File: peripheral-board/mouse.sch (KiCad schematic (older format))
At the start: 3 parts

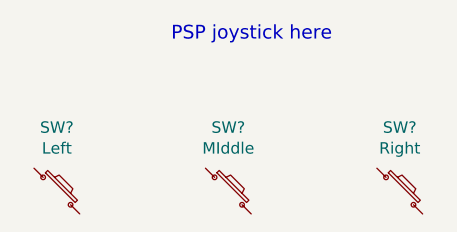
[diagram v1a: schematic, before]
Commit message: added button 3d model
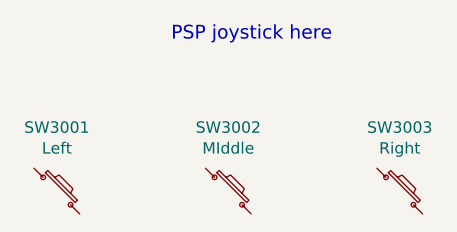
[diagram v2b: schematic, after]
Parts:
- SW3001, SW3002, SW3003: renamed from SW?; footprint (none) -> lib:SMD-TACT-5.2x5.2x2mm
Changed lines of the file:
@@
 PSP joystick here\n
 $Comp
-L SW_PUSH_Small SW?
+L SW_PUSH_Small SW3001
 U 1 1 5819E7E8
 P 4500 4450
-F 0 "SW?" H 4500 4728 50  0000 C CNN
+F 0 "SW3001" H 4500 4728 50  0000 C CNN
 F 1 "Left" H 4500 4637 50  0000 C CNN
-F 2 "" H 4500 4450 50  0000 C CNN
+F 2 "lib:SMD-TACT-5.2x5.2x2mm" H 4500 4450 50  0001 C CNN
 F 3 "" H 4500 4450 50  0000 C CNN
 	1    4500 4450
@@
 $EndComp
 $Comp
-L SW_PUSH_Small SW?
+L SW_PUSH_Small SW3003
 U 1 1 5819E880
 P 6000 4450
-F 0 "SW?" H 6000 4728 50  0000 C CNN
+F 0 "SW3003" H 6000 4728 50  0000 C CNN
 F 1 "Right" H 6000 4637 50  0000 C CNN
-F 2 "" H 6000 4450 50  0000 C CNN
+F 2 "lib:SMD-TACT-5.2x5.2x2mm" H 6000 4450 50  0001 C CNN
 F 3 "" H 6000 4450 50  0000 C CNN
 	1    6000 4450
@@
 $EndComp
 $Comp
-L SW_PUSH_Small SW?
+L SW_PUSH_Small SW3002
 U 1 1 5819E8E2
 P 5250 4450
-F 0 "SW?" H 5250 4728 50  0000 C CNN
+F 0 "SW3002" H 5250 4728 50  0000 C CNN
 F 1 "MIddle" H 5250 4637 50  0000 C CNN
-F 2 "" H 5250 4450 50  0000 C CNN
+F 2 "lib:SMD-TACT-5.2x5.2x2mm" H 5250 4450 50  0001 C CNN
 F 3 "" H 5250 4450 50  0000 C CNN
 	1    5250 4450

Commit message: added keyboard scanning logic
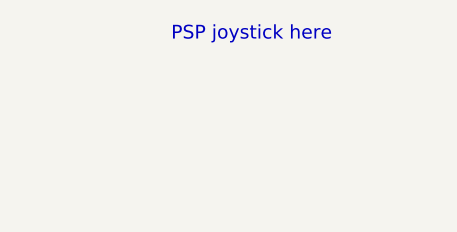
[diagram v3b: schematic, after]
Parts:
- removed SW3001: Left, lib:SMD-TACT-5.2x5.2x2mm, symbol SW_PUSH_Small
- removed SW3002: MIddle, lib:SMD-TACT-5.2x5.2x2mm, symbol SW_PUSH_Small
- removed SW3003: Right, lib:SMD-TACT-5.2x5.2x2mm, symbol SW_PUSH_Small
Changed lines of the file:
@@
 Text Notes 5000 3800 0    60   ~ 0
 PSP joystick here\n
-$Comp
-L SW_PUSH_Small SW3001
-U 1 1 5819E7E8
-P 4500 4450
-F 0 "SW3001" H 4500 4728 50  0000 C CNN
-F 1 "Left" H 4500 4637 50  0000 C CNN
-F 2 "lib:SMD-TACT-5.2x5.2x2mm" H 4500 4450 50  0001 C CNN
-F 3 "" H 4500 4450 50  0000 C CNN
-	1    4500 4450
-	1    0    0    -1
-$EndComp
-$Comp
-L SW_PUSH_Small SW3003
-U 1 1 5819E880
-P 6000 4450
-F 0 "SW3003" H 6000 4728 50  0000 C CNN
-F 1 "Right" H 6000 4637 50  0000 C CNN
-F 2 "lib:SMD-TACT-5.2x5.2x2mm" H 6000 4450 50  0001 C CNN
-F 3 "" H 6000 4450 50  0000 C CNN
-	1    6000 4450
-	1    0    0    -1
-$EndComp
-$Comp
-L SW_PUSH_Small SW3002
-U 1 1 5819E8E2
-P 5250 4450
-F 0 "SW3002" H 5250 4728 50  0000 C CNN
-F 1 "MIddle" H 5250 4637 50  0000 C CNN
-F 2 "lib:SMD-TACT-5.2x5.2x2mm" H 5250 4450 50  0001 C CNN
-F 3 "" H 5250 4450 50  0000 C CNN
-	1    5250 4450
-	1    0    0    -1
-$EndComp
 $EndSCHEMATC

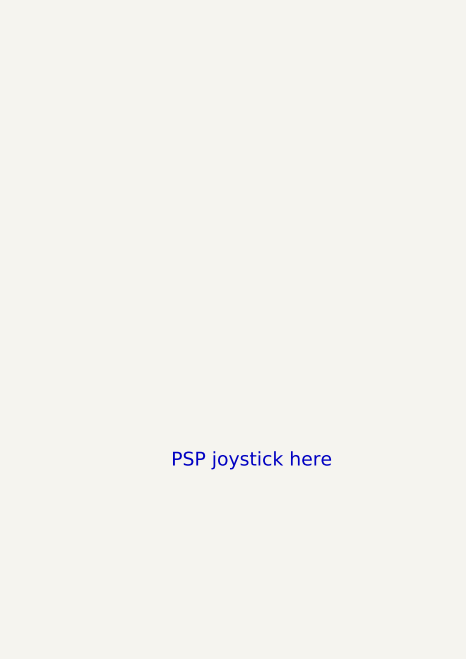
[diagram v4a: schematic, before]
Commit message: routed keyboard
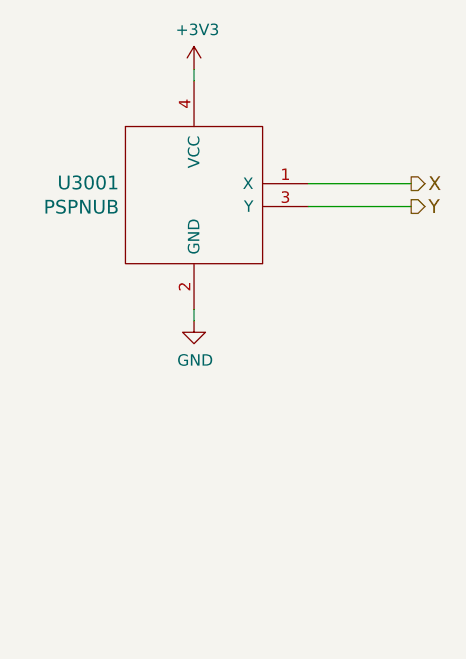
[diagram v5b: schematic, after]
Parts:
- added U3001: PSPNUB, symbol PSPNUB
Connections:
- new net +3V3: U3001.4 (VCC)
- new net GND: U3001.2 (GND)
- new net X: U3001.1 (X)
- new net Y: U3001.3 (Y)
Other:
- note removed: "PSP joystick here\n"
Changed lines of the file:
@@
 LIBS:amp
 LIBS:card-edge
+LIBS:switchmode
+LIBS:joystick
 LIBS:peripheral-board-cache
 EELAYER 25 0
@@
 Comment4 ""
 $EndDescr
-Text Notes 5000 3800 0    60   ~ 0
-PSP joystick here\n
+$Comp
+L PSPNUB U3001
+U 1 1 5822698D
+P 5100 2600
+F 0 "U3001" H 4772 2653 60  0000 R CNN
+F 1 "PSPNUB" H 4772 2547 60  0000 R CNN
+F 2 "" H 5100 2600 60  0001 C CNN
+F 3 "" H 5100 2600 60  0001 C CNN
+	1    5100 2600
+	1    0    0    -1
+$EndComp
+$Comp
+L +3V3 #PWR022
+U 1 1 582269F3
+P 5100 2050
+F 0 "#PWR022" H 5100 1900 50  0001 C CNN
+F 1 "+3V3" H 5115 2223 50  0000 C CNN
+F 2 "" H 5100 2050 50  0000 C CNN
+F 3 "" H 5100 2050 50  0000 C CNN
+	1    5100 2050
+	1    0    0    -1
+$EndComp
+$Comp
+L GND #PWR023
+U 1 1 58226A0A
+P 5100 3150
+F 0 "#PWR023" H 5100 2900 50  0001 C CNN
+F 1 "GND" H 5105 2977 50  0000 C CNN
+F 2 "" H 5100 3150 50  0000 C CNN
+F 3 "" H 5100 3150 50  0000 C CNN
+	1    5100 3150
+	1    0    0    -1
+$EndComp
+Wire Wire Line
+	5100 2050 5100 2100
+Wire Wire Line
+	5100 3100 5100 3150
+Text HLabel 6050 2550 2    60   Output ~ 0
+X
+Text HLabel 6050 2650 2    60   Output ~ 0
+Y
+Wire Wire Line
+	6050 2550 5600 2550
+Wire Wire Line
+	5600 2650 6050 2650
 $EndSCHEMATC

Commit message: added some audio circuitry
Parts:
- U3001: footprint (none) -> lib:PSPNUB
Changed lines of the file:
@@
 LIBS:switchmode
 LIBS:joystick
+LIBS:digital-pot
 LIBS:peripheral-board-cache
-EELAYER 25 0
+EELAYER 26 0
 EELAYER END
 $Descr A4 11693 8268
@@
 F 0 "U3001" H 4772 2653 60  0000 R CNN
 F 1 "PSPNUB" H 4772 2547 60  0000 R CNN
-F 2 "" H 5100 2600 60  0001 C CNN
+F 2 "lib:PSPNUB" H 5100 2600 60  0001 C CNN
 F 3 "" H 5100 2600 60  0001 C CNN
 	1    5100 2600
